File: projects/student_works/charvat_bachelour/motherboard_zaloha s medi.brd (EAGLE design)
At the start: 86.4 x 106.7 mm, 17 parts

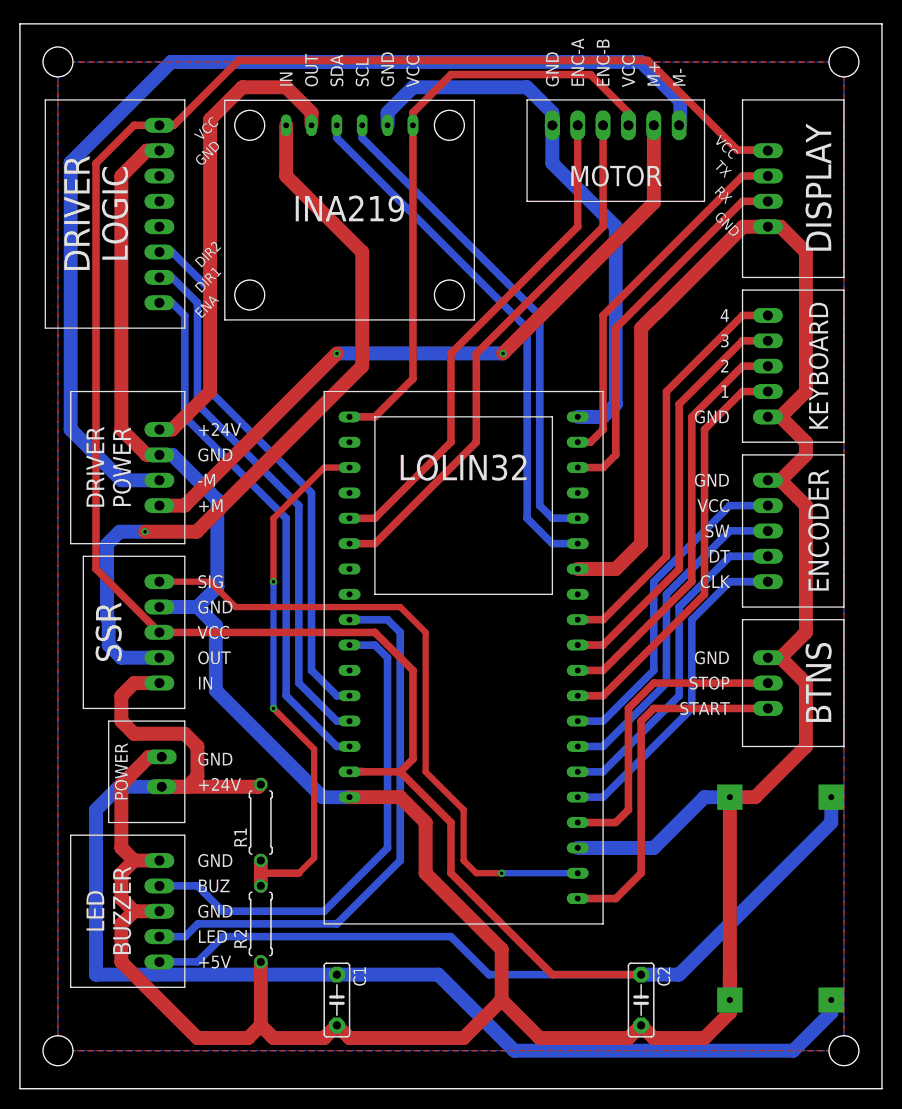
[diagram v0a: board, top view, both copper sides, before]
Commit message: charvat bakalarka minor fixes
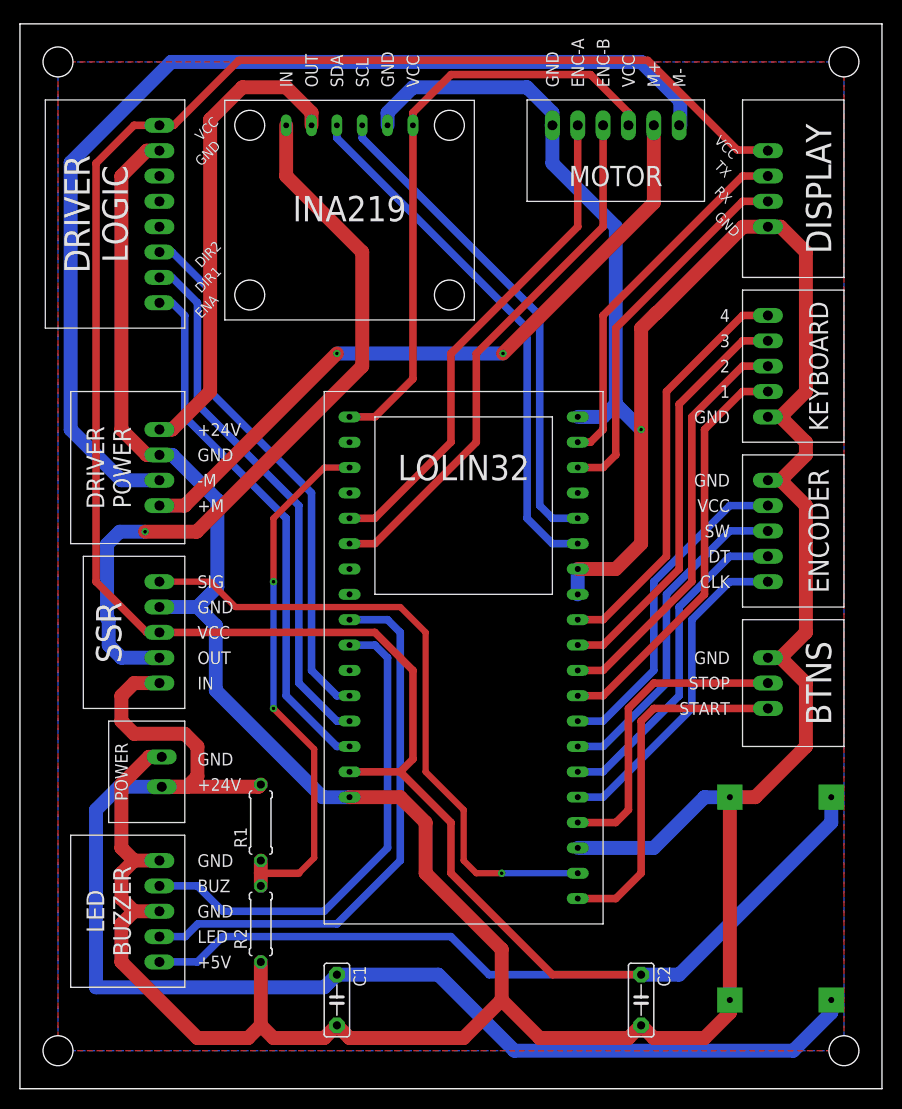
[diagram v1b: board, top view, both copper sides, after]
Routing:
- net GND: track 440.5 -> 444.0 mm, vias 0 -> 1
- net N$21: track 136.3 -> 138.1 mm
- net +5V: track 283.3 -> 282.8 mm
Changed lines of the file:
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@@
 <contactref element="U$7" pad="VCC"/>
 <contactref element="U$1" pad="+5V"/>
-<wire x1="34.29" y1="31.8008" x2="33.02" y2="31.75" width="0.762" layer="1"/>
 <wire x1="71.882" y1="94.0435" x2="74.9046" y2="94.0435" width="0.762" layer="1"/>
 <wire x1="62.9031" y1="103.0224" x2="71.882" y2="94.0435" width="0.762" layer="1"/>
@@
 <wire x1="39.37" y1="41.91" x2="35.56" y2="45.72" width="0.762" layer="1"/>
 <wire x1="35.56" y1="45.72" x2="13.97" y2="45.72" width="0.762" layer="1"/>
-<wire x1="13.97" y1="45.72" x2="7.62" y2="52.07" width="0.762" layer="1"/>
-<wire x1="7.62" y1="52.07" x2="7.62" y2="92.71" width="0.762" layer="1"/>
+<wire x1="13.97" y1="45.72" x2="12.7" y2="45.72" width="0.762" layer="1"/>
+<wire x1="12.7" y1="45.72" x2="7.62" y2="50.8" width="0.762" layer="1"/>
+<wire x1="7.62" y1="50.8" x2="7.62" y2="92.71" width="0.762" layer="1"/>
 <wire x1="7.62" y1="92.71" x2="11.43" y2="96.52" width="0.762" layer="1"/>
 <wire x1="11.43" y1="96.52" x2="13.97" y2="96.52" width="0.762" layer="1"/>
@@
 <contactref element="U$8" pad="32"/>
 <contactref element="U$3" pad="B"/>
-<wire x1="55.753" y1="96.52" x2="55.88" y2="96.52" width="0.508" layer="1"/>
 <wire x1="33.02" y1="57.15" x2="35.56" y2="57.15" width="0.762" layer="1"/>
 <wire x1="35.56" y1="57.15" x2="43.18" y2="64.77" width="0.762" layer="1"/>
@@
 <wire x1="66.1543" y1="98.9457" x2="66.1543" y2="98.99015" width="1.397" layer="16"/>
 <wire x1="15.1511" y1="102.87" x2="62.23" y2="102.87" width="1.397" layer="16"/>
-<wire x1="66.1543" y1="98.9457" x2="66.1543" y2="96.52" width="1.397" layer="16"/>
+<wire x1="66.1543" y1="96.52" x2="66.1543" y2="98.9457" width="1.397" layer="16"/>
 <wire x1="5.08" y1="92.7989" x2="15.1511" y2="102.87" width="1.397" layer="16"/>
 <wire x1="62.23" y1="102.87" x2="66.1543" y2="98.9457" width="1.397" layer="16"/>
-<wire x1="66.1543" y1="96.52" x2="66.04" y2="96.52" width="0" layer="19" extent="16-16"/>
+<wire x1="66.04" y1="96.52" x2="66.1543" y2="96.52" width="1.397" layer="16"/>
 </signal>
 <signal name="N$4" class="3">
@@
 <signal name="N$22">
 <contactref element="U$2" pad="SDA"/>
-<wire x1="31.75" y1="96.52" x2="31.8135" y2="96.4565" width="0.508" layer="16"/>
 <contactref element="U$8" pad="21"/>
 <wire x1="55.88" y1="54.61" x2="53.34" y2="54.61" width="0.762" layer="16"/>
@@
 <wire x1="14.2" y1="30.25" x2="9.93" y2="30.25" width="1.397" layer="16"/>
 <wire x1="9.93" y1="30.25" x2="7.62" y2="27.94" width="1.397" layer="16"/>
-<wire x1="7.62" y1="27.94" x2="7.62" y2="11.43" width="1.397" layer="16"/>
-<wire x1="7.62" y1="11.43" x2="31.75" y2="11.43" width="1.397" layer="16"/>
+<wire x1="7.62" y1="27.94" x2="7.62" y2="10.16" width="1.397" layer="16"/>
+<wire x1="30.48" y1="10.16" x2="7.62" y2="10.16" width="1.397" layer="16"/>
+<wire x1="30.48" y1="10.16" x2="31.75" y2="11.43" width="1.397" layer="16"/>
 <wire x1="31.75" y1="11.43" x2="41.91" y2="11.43" width="1.397" layer="16"/>
 <wire x1="81.28" y1="8.89" x2="81.28" y2="7.62" width="1.397" layer="16"/>
@@
 <contactref element="U$8" pad="4"/>
 <contactref element="U$6" pad="CLK"/>
-<wire x1="74.9046" y1="50.7619" x2="74.93" y2="50.8" width="0.508" layer="1"/>
 <wire x1="55.88" y1="29.21" x2="58.42" y2="29.21" width="0.762" layer="16"/>
 <wire x1="58.42" y1="29.21" x2="67.31" y2="38.1" width="0.762" layer="16"/>
@@
 <contactref element="U$6" pad="GND"/>
 <contactref element="U$13" pad="GND"/>
-<wire x1="74.9046" y1="67.31" x2="74.93" y2="67.31" width="0.508" layer="1"/>
 <contactref element="U$8" pad="GND_3"/>
 <contactref element="U$8" pad="GND_2"/>
@@
 <contactref element="U$2" pad="GND"/>
 <wire x1="53.2765" y1="96.52" x2="53.34" y2="96.52" width="1.397" layer="16"/>
-<wire x1="59.69" y1="68.58" x2="58.42" y2="67.31" width="1.397" layer="16"/>
+<wire x1="58.42" y1="67.31" x2="59.69" y2="68.58" width="1.397" layer="16"/>
 <wire x1="58.42" y1="67.31" x2="55.88" y2="67.31" width="1.397" layer="16"/>
 <wire x1="53.34" y1="96.52" x2="53.34" y2="92.71" width="1.397" layer="16"/>
@@
 <wire x1="55.88" y1="52.07" x2="59.69" y2="52.07" width="1.397" layer="1"/>
 <wire x1="59.69" y1="52.07" x2="62.23" y2="54.61" width="1.397" layer="1"/>
-<wire x1="62.23" y1="54.61" x2="62.23" y2="76.2" width="1.397" layer="1"/>
+<wire x1="62.23" y1="54.61" x2="62.23" y2="66.04" width="1.397" layer="1"/>
+<wire x1="62.23" y1="66.04" x2="62.23" y2="76.2" width="1.397" layer="1"/>
 <wire x1="62.23" y1="76.2" x2="63.7667" y2="77.7367" width="1.397" layer="1"/>
 <wire x1="63.7667" y1="77.7367" x2="63.8175" y2="77.7367" width="1.397" layer="1"/>
@@
 <wire x1="68.58" y1="5.08" x2="71.12" y2="7.62" width="1.397" layer="1"/>
 <wire x1="71.12" y1="7.62" x2="71.12" y2="8.89" width="1.397" layer="1"/>
-<wire x1="71.12" y1="11.43" x2="71.12" y2="8.89" width="1.397" layer="1"/>
 <wire x1="71.12" y1="29.21" x2="71.12" y2="8.89" width="1.397" layer="1"/>
 <wire x1="31.75" y1="6.35" x2="30.48" y2="5.08" width="1.397" layer="1"/>
@@
 <wire x1="33.02" y1="5.08" x2="44.45" y2="5.08" width="1.397" layer="1"/>
 <wire x1="44.45" y1="5.08" x2="48.26" y2="8.89" width="1.397" layer="1"/>
+<wire x1="55.88" y1="52.07" x2="55.88" y2="49.53" width="1.397" layer="16"/>
+<wire x1="59.69" y1="68.58" x2="62.23" y2="66.04" width="1.397" layer="16"/>
+<via x="62.23" y="66.04" extent="1-16" drill="0.35"/>
 </signal>
 <signal name="N$38">
@@
 <contactref element="U$8" pad="12"/>
 <contactref element="U$10" pad="IN1"/>
-<wire x1="13.8176" y1="81.1657" x2="13.97" y2="81.28" width="0.508" layer="16"/>
 <wire x1="33.02" y1="36.83" x2="31.75" y2="36.83" width="0.762" layer="16"/>
 <wire x1="31.75" y1="36.83" x2="27.94" y2="40.64" width="0.762" layer="16"/>
